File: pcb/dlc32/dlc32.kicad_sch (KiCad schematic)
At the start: 30 parts, among them IC1 74HCT08, IC2 74HCT04, J1 DOOR1, J12 Conn_01x03, J13 Conn_01x03, J2 DOOR2, J3 CHILLER_OK, J7 LASER_AUX, J8 LASER

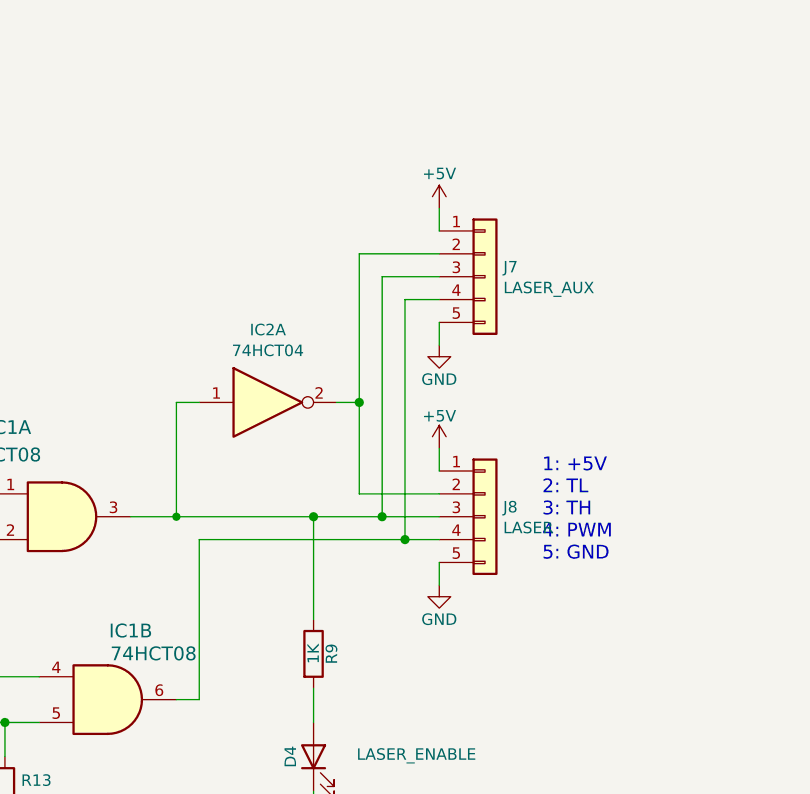
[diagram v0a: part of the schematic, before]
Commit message: Fix footprint for R1.
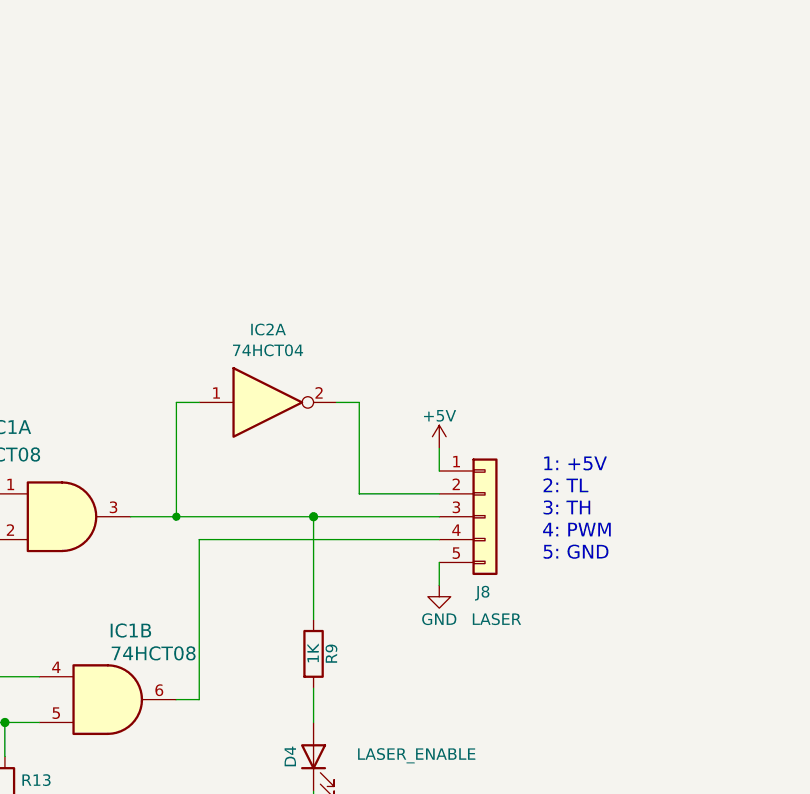
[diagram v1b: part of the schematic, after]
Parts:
- removed J7: LASER_AUX, Connector_JST:JST_XH_B5B-XH-A_1x05_P2.50mm_Vertical, symbol Connector_Generic:Conn_01x05
- J12: value Conn_01x03 -> DOORJMP1
- J13: value Conn_01x03 -> DOORJMP2
- R1: footprint PCM_Resistor_SMD_AKL:R_Array_Concave_4x0603 -> PCM_Resistor_SMD_AKL:R_Array_Convex_4x0603

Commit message: Route some more.
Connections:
- net LASER_EN: now also IC1.12; no longer IC1.1
- net at IC2.1, J8.3 (Pin_3), R9.1: now also IC1.11; no longer IC1.3
- net at C1.1, R8.1: now also IC1.1; no longer IC1.12
- net at IC1.8, IC2.13: now also IC1.2; no longer IC1.13
- new net: IC1.13, IC1.3, IC1.4
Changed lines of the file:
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@@
 		(lib_id "74xx:74LS08")
 		(at 189.23 85.09 0)
-		(unit 1)
+		(unit 4)
 		(exclude_from_sim no)
 		(in_bom yes)
@@
 				(path "/fc0b2ef6-7d8e-4322-8468-8fac0c3c3d07"
 					(reference "IC1")
-					(unit 1)
+					(unit 4)
 				)
 			)
@@
 		(lib_id "74xx:74LS08")
 		(at 157.48 87.63 0)
-		(unit 4)
+		(unit 1)
 		(exclude_from_sim no)
 		(in_bom yes)
@@
 				(path "/fc0b2ef6-7d8e-4322-8468-8fac0c3c3d07"
 					(reference "IC1")
-					(unit 4)
-				)
-			)
+					(unit 1)
+				)
+			)

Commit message: Route.
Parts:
- added H5, H6: MountingHole, MountingHole:MountingHole_3.2mm_M3, symbol Mechanical:MountingHole
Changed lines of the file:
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@@
+	)
+	(symbol
+		(lib_id "Mechanical:MountingHole")
+		(at 58.42 36.83 0)
+		(unit 1)
+		(exclude_from_sim yes)
+		(in_bom no)
+		(on_board yes)
+		(dnp no)
+		(fields_autoplaced yes)
+		(property "Reference" "H6"
+			(at 60.96 35.5599 0)
+			(effects
+				(font
+					(size 1.27 1.27)
+				)
+				(justify left)
+			)
+		)
+		(property "Value" "MountingHole"
+			(at 60.96 38.0999 0)
+			(effects
+				(font
+					(size 1.27 1.27)
+				)
+				(justify left)
+			)
+		)
+		(property "Footprint" "MountingHole:MountingHole_3.2mm_M3"
+			(at 58.42 36.83 0)
+			(effects
+				(font
+					(size 1.27 1.27)
+				)
+				(hide yes)
+			)
+		)
+		(property "Datasheet" "~"
+			(at 58.42 36.83 0)
+			(effects
+				(font
+					(size 1.27 1.27)
+				)
+				(hide yes)
+			)
+		)
+		(property "Description" "Mounting Hole without connection"
+			(at 58.42 36.83 0)
+			(effects
+				(font
+					(size 1.27 1.27)
+				)
+				(hide yes)
+			)
+		)
+		(instances
+			(project "dlc32"
+				(path "/fc0b2ef6-7d8e-4322-8468-8fac0c3c3d07"
+					(reference "H6")
+					(unit 1)
+				)
+			)
+		)
 	)
 	(symbol
@@
 					(unit 1)
 				)
+			)
+		)
+	)
+	(symbol
+		(lib_id "Mechanical:MountingHole")
+		(at 58.42 30.48 0)
+		(unit 1)
+		(exclude_from_sim yes)
+		(in_bom no)
+		(on_board yes)
+		(dnp no)
+		(fields_autoplaced yes)
+		(property "Reference" "H5"
+			(at 60.96 29.2099 0)
+			(effects
+				(font
+					(size 1.27 1.27)
+				)
+				(justify left)
+			)
+		)
+		(property "Value" "MountingHole"
+			(at 60.96 31.7499 0)
+			(effects
+				(font
+					(size 1.27 1.27)
+				)
+				(justify left)
+			)
+		)
+		(property "Footprint" "MountingHole:MountingHole_3.2mm_M3"
+			(at 58.42 30.48 0)
+			(effects
+				(font
+					(size 1.27 1.27)
+				)
+				(hide yes)
+			)
+		)
+		(property "Datasheet" "~"
+			(at 58.42 30.48 0)
+			(effects
+				(font
+					(size 1.27 1.27)
+				)
+				(hide yes)
+			)
+		)
+		(property "Description" "Mounting Hole without connection"
+			(at 58.42 30.48 0)
+			(effects
+				(font
+					(size 1.27 1.27)
+				)
+				(hide yes)
+			)
+		)
+		(instances
+			(project "dlc32"
+				(path "/fc0b2ef6-7d8e-4322-8468-8fac0c3c3d07"
+					(reference "H5")
+					(unit 1)
+				)

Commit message: Make pretty.
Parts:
- D3: value LED -> CHILLER OK
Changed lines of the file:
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@@
 			)
 		)
-		(property "Value" "LED"
+		(property "Value" "CHILLER OK"
 			(at 112.0775 62.23 0)
 			(effects

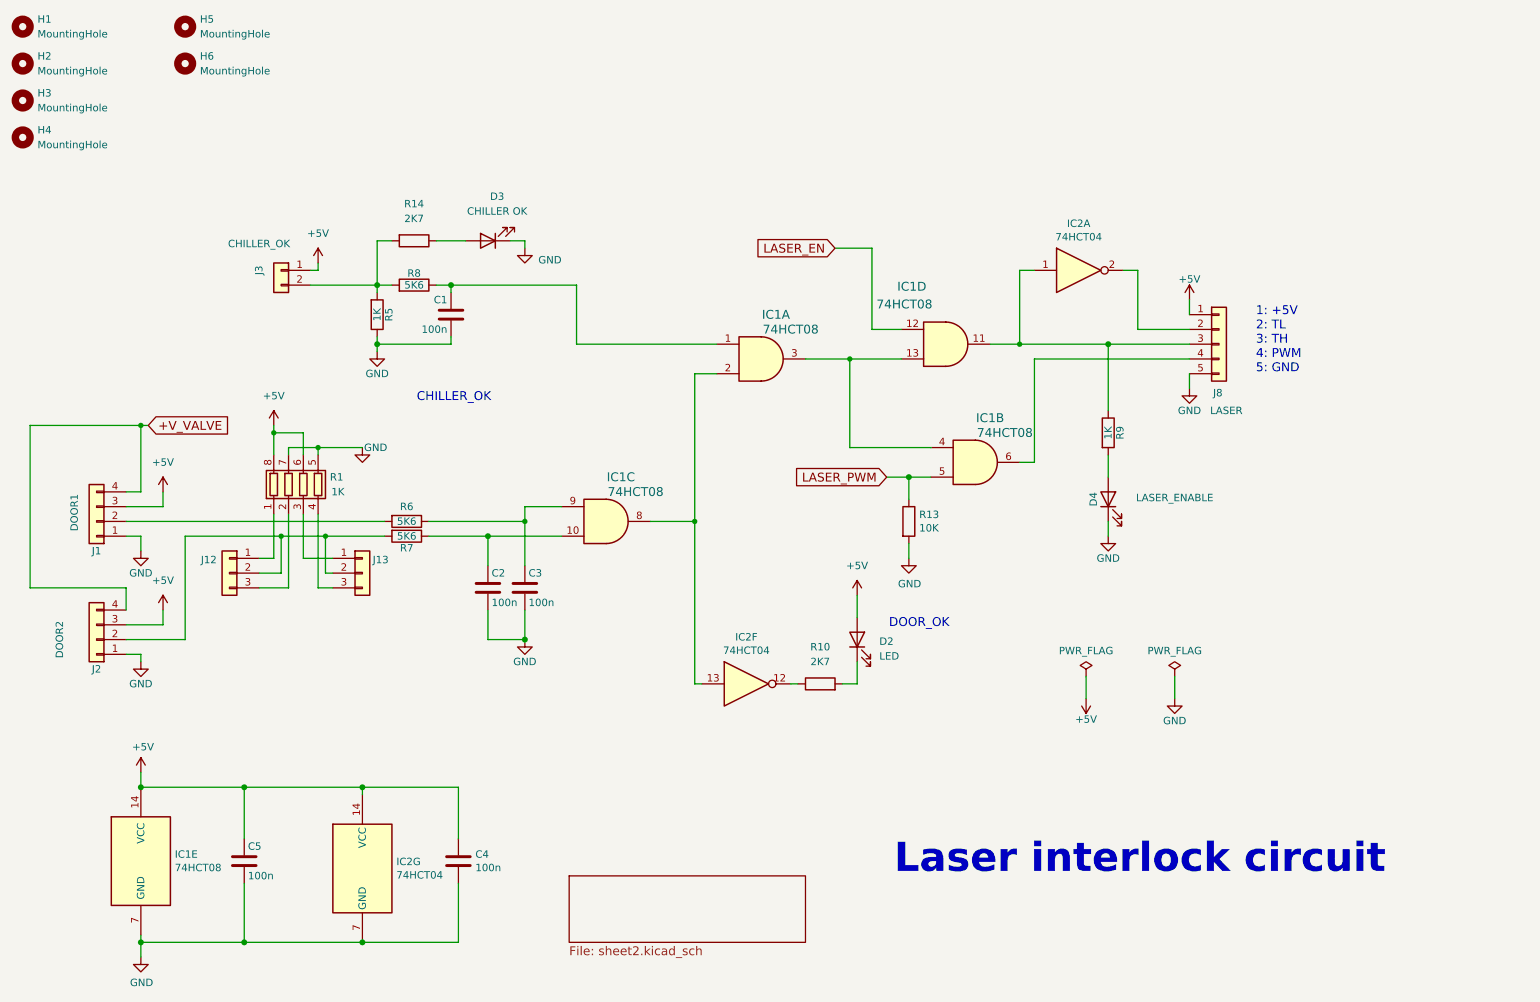
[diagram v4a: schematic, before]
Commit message: Use Schmitt triggers. Add clamping diodes, test point.
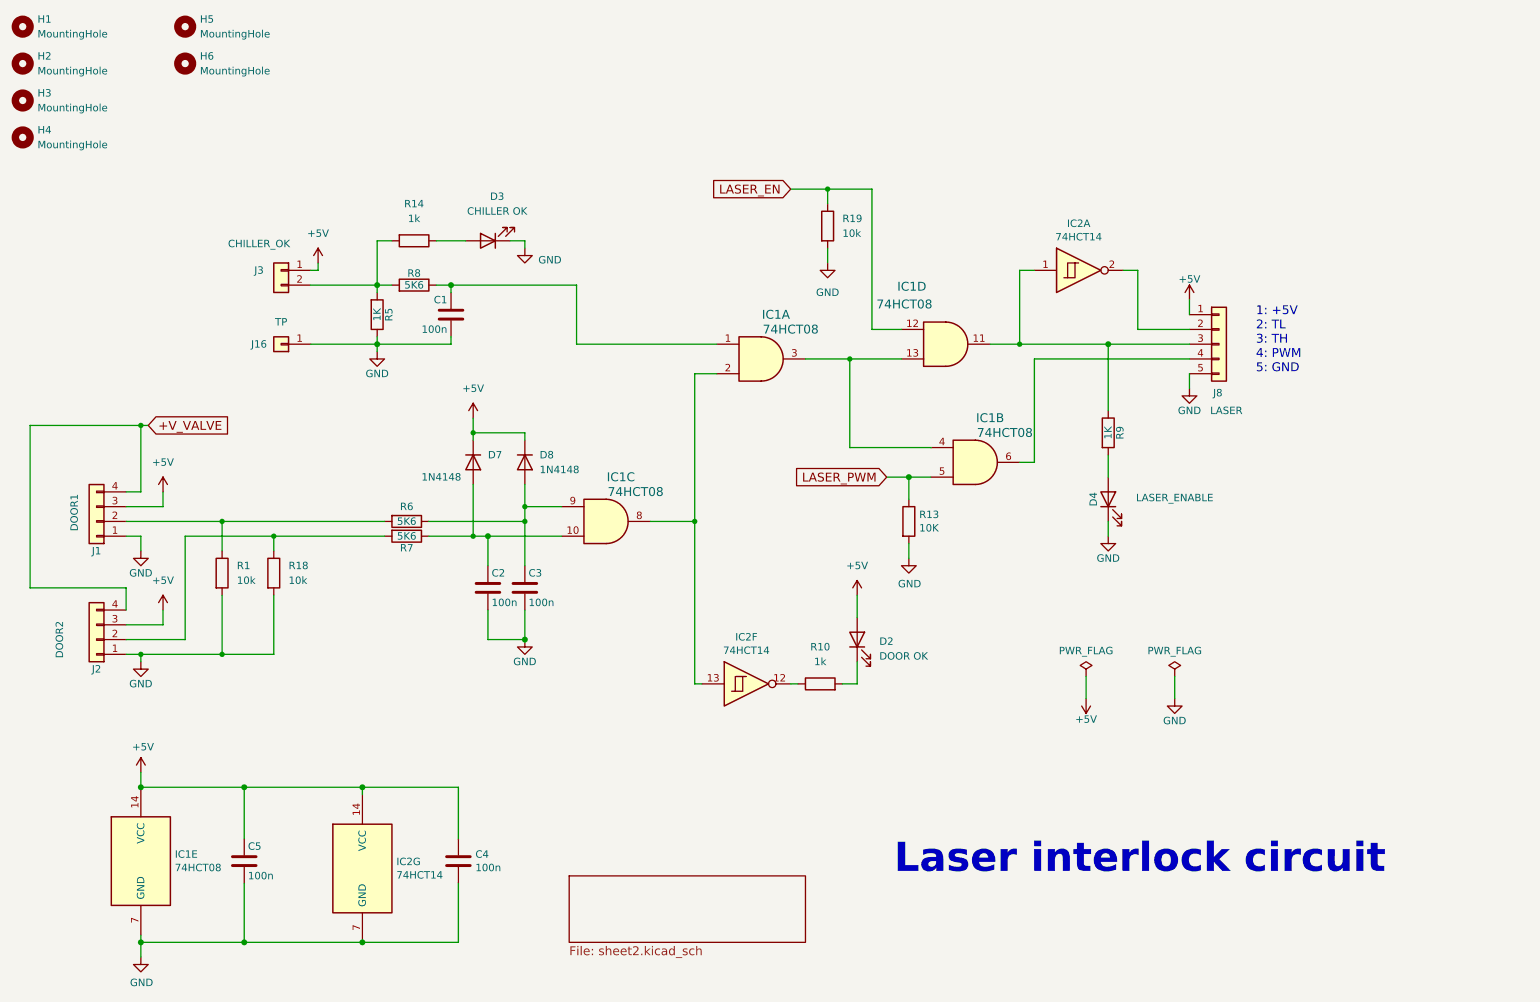
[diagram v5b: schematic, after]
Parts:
- removed J12: DOORJMP1, Connector_PinHeader_2.54mm:PinHeader_1x03_P2.54mm_Vertical, symbol Connector_Generic:Conn_01x03
- removed J13: DOORJMP2, Connector_PinHeader_2.54mm:PinHeader_1x03_P2.54mm_Vertical, symbol Connector_Generic:Conn_01x03
- removed R1: 1K, PCM_Resistor_SMD_AKL:R_Array_Convex_4x0603, symbol Device:R_Pack04
- added D7, D8: 1N4148, PCM_Diode_SMD_AKL:D_MiniMELF, symbol Device:D
- added J16: TP, TestPoint:TestPoint_Loop_D1.80mm_Drill1.0mm_Beaded, symbol Connector_Generic:Conn_01x01
- added R1, R18, R19: 10k, PCM_Resistor_SMD_AKL:R_0603_1608Metric, symbol Device:R
- D2: value LED -> DOOR OK
- IC2: value 74HCT04 -> 74HCT14; symbol 74xx:74HCT04 -> 74xx:74HC14
- R10, R14: value 2K7 -> 1k
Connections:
- net +5V: now also D7.1 (K), D8.1 (K)
- net GND: now also J16.1 (Pin_1), R1.2, R18.2, R19.2
- net LASER_EN: now also R19.1
- net at C3.1, IC1.9, R6.1: now also D8.2 (A)
- net at J1.2 (Pin_2), R6.2: now also R1.1
- net at C2.1, IC1.10, R7.1: now also D7.2 (A)
- net at J2.2 (Pin_2), R7.2: now also R18.1
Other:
- note removed: "CHILLER_OK"
- note removed: "DOOR_OK"

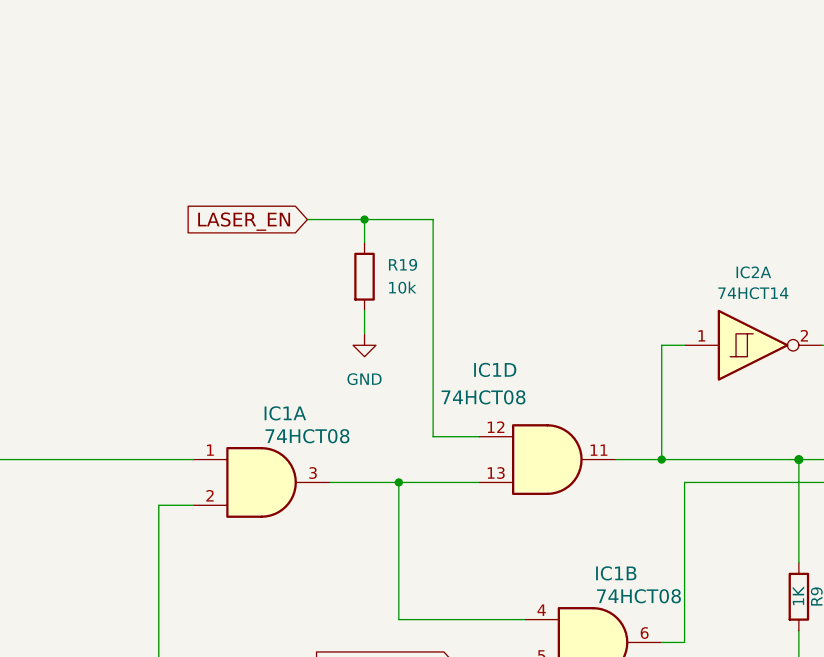
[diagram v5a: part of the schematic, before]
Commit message: Eliminate LASER_EN.
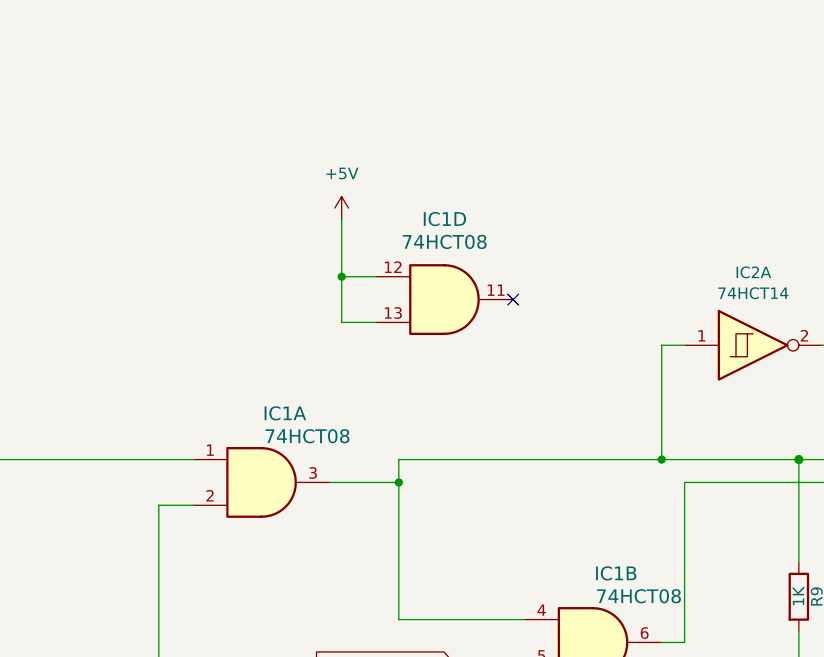
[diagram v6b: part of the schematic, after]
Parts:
- removed R19: 10k, PCM_Resistor_SMD_AKL:R_0603_1608Metric, symbol Device:R
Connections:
- net LASER_EN is gone; now on net +5V: IC1.12
- net +5V: now also IC1.13
- net at IC2.1, J8.3 (Pin_3), R9.1: now also IC1.3, IC1.4; no longer IC1.11
- no-connect marks 0 -> 1
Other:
- moved on the sheet: IC1D

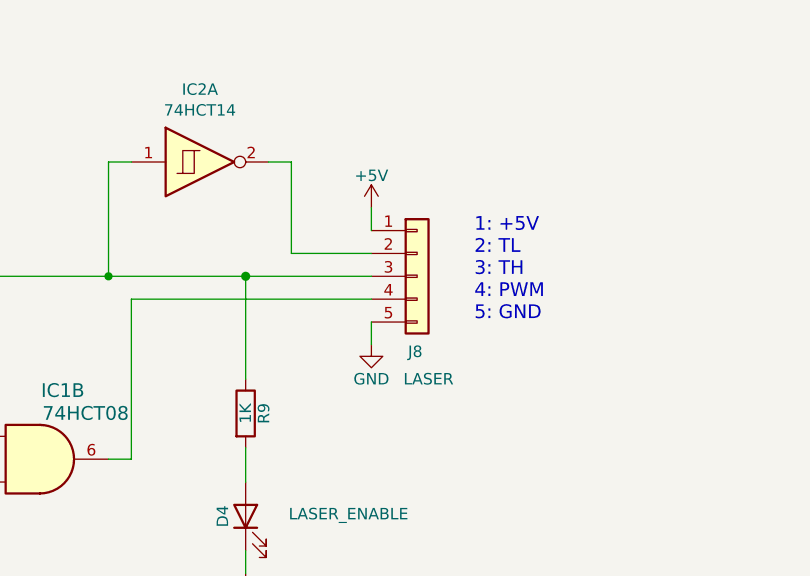
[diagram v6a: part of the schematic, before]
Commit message: Update laser connector, prevent fan activation on startup.
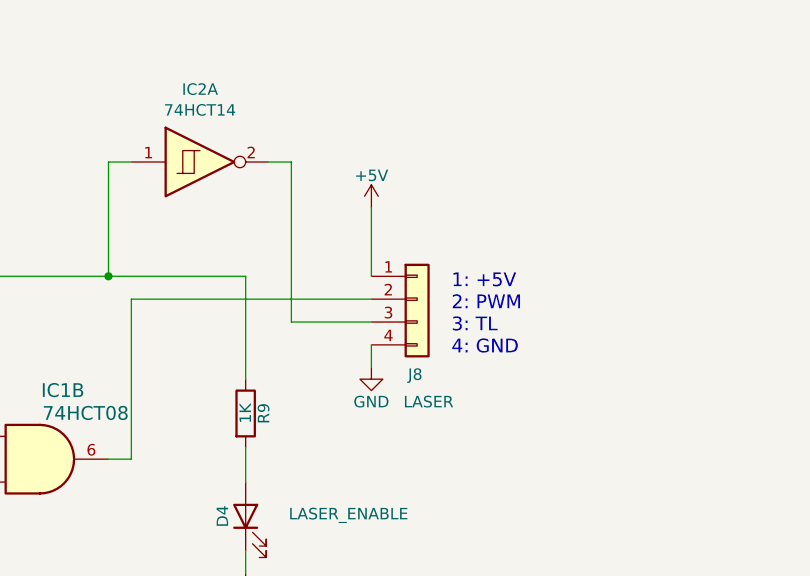
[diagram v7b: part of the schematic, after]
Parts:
- J8: symbol Connector_Generic:Conn_01x05 -> Connector_Generic:Conn_01x04
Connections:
- net GND: now also J8.4 (Pin_4); no longer J8.5 (Pin_5)
- net at IC1.3, IC1.4, IC2.1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: no longer J8.3 (Pin_3)
- net at IC1.6: now also J8.2 (Pin_2); no longer J8.4 (Pin_4)
- net at IC2.2: now also J8.3 (Pin_3); no longer J8.2 (Pin_2)
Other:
- note added: "1: +5V 2: PWM 3: TL 4: GND"
- note removed: "1: +5V 2: TL 3: TH 4: PWM 5: GND"
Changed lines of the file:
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@@
 		)
 	)
-	(text "1: +5V\n2: TL\n3: TH\n4: PWM\n5: GND"
+	(text "1: +5V\n2: PWM\n3: TL\n4: GND"
 		(exclude_from_sim no)
-		(at 242.57 90.17 0)
+		(at 240.03 93.98 0)
 		(effects
 			(font
@@
 	)
 	(junction
-		(at 217.17 85.09)
-		(diameter 1.016)
-		(color 0 0 0 0)
-	)
-	(junction
 		(at 107.95 118.11)
 		(diameter 0)
@@
 	(wire
 		(pts
+			(xy 222.25 90.17) (xy 231.14 90.17)
+		)
+		(stroke
+			(width 0)
+			(type solid)
+		)
+	)
+	(wire
+		(pts
 			(xy 165.1 87.63) (xy 172.72 87.63)
 		)
@@
 	(wire
 		(pts
-			(xy 231.14 77.47) (xy 231.14 80.01)
-		)
-		(stroke
-			(width 0)
-			(type solid)
-		)
-	)
-	(wire
-		(pts
 			(xy 105.41 177.8) (xy 105.41 187.96)
 		)
@@
 	(wire
 		(pts
+			(xy 231.14 77.47) (xy 231.14 85.09)
+		)
+		(stroke
+			(width 0)
+			(type solid)
+		)
+	)
+	(wire
+		(pts
 			(xy 166.37 69.85) (xy 170.18 69.85)
 		)
@@
 	(wire
 		(pts
-			(xy 149.86 85.09) (xy 125.73 85.09)
+			(xy 231.14 92.71) (xy 231.14 95.25)
 		)
 		(stroke
@@
 	(wire
 		(pts
-			(xy 116.84 100.33) (xy 107.95 100.33)
+			(xy 149.86 85.09) (xy 125.73 85.09)
 		)
 		(stroke
@@
 	(wire
 		(pts
-			(xy 116.84 113.03) (xy 116.84 115.57)
+			(xy 116.84 100.33) (xy 107.95 100.33)
 		)
 		(stroke
@@
 	(wire
 		(pts
-			(xy 217.17 115.57) (xy 217.17 118.11)
+			(xy 116.84 113.03) (xy 116.84 115.57)
 		)
 		(stroke
 			(width 0)
-			(type solid)
+			(type default)
 		)
 	)
 	(wire
 		(pts
-			(xy 217.17 85.09) (xy 231.14 85.09)
+			(xy 217.17 115.57) (xy 217.17 118.11)
 		)
 		(stroke
@@
 	(wire
 		(pts
-			(xy 222.25 82.55) (xy 231.14 82.55)
-		)
-		(stroke
-			(width 0)
-			(type solid)
-		)
-	)
-	(wire
-		(pts
 			(xy 50.8 110.49) (xy 48.26 110.49)
 		)
@@
 	(wire
 		(pts
-			(xy 222.25 72.39) (xy 222.25 82.55)
-		)
-		(stroke
-			(width 0)
-			(type solid)
-		)
-	)
-	(wire
-		(pts
-			(xy 231.14 90.17) (xy 231.14 92.71)
+			(xy 222.25 72.39) (xy 222.25 90.17)
 		)
 		(stroke
@@
 	(symbol
 		(lib_id "power:GND")
-		(at 231.14 92.71 0)
+		(at 231.14 95.25 0)
 		(unit 1)
 		(exclude_from_sim no)
@@
 		(dnp no)
 		(property "Reference" "#PWR05"
-			(at 231.14 99.06 0)
+			(at 231.14 101.6 0)
 			(effects
 				(font
@@
 		)
 		(property "Value" "GND"
-			(at 231.14 96.52 0)
+			(at 231.14 99.06 0)
 			(effects
 				(font
@@
 		)
 		(property "Footprint" ""
-			(at 231.14 92.71 0)
+			(at 231.14 95.25 0)
 			(effects
 				(font
@@
 		)
 		(property "Datasheet" ""
-			(at 231.14 92.71 0)
+			(at 231.14 95.25 0)
 			(effects
 				(font
@@
 		)
 		(property "Description" "Power symbol creates a global label with name \"GND\" , ground"
-			(at 231.14 92.71 0)
+			(at 231.14 95.25 0)
 			(effects
 				(font
@@
 	)
 	(symbol
-		(lib_id "Connector_Generic:Conn_01x05")
-		(at 236.22 85.09 0)
+		(lib_id "Connector_Generic:Conn_01x04")
+		(at 236.22 87.63 0)
 		(unit 1)
 		(exclude_from_sim no)
@@
 		(dnp no)
 		(property "Reference" "J8"
-			(at 235.204 93.472 0)
+			(at 235.204 96.012 0)
 			(effects
 				(font
@@
 		)
 		(property "Value" "LASER"
-			(at 234.696 96.52 0)
+			(at 234.696 99.06 0)
 			(effects
 				(font
@@
 		)
 		(property "Footprint" "Connector_JST:JST_XH_B5B-XH-A_1x05_P2.50mm_Vertical"
-			(at 236.22 85.09 0)
+			(at 236.22 87.63 0)
 			(effects
 				(font
@@
 		)
 		(property "Datasheet" "~"
-			(at 236.22 85.09 0)
+			(at 236.22 87.63 0)
 			(effects
 				(font
@@
 			)
 		)
-		(property "Description" ""
-			(at 236.22 85.09 0)
+		(property "Description" "Generic connector, single row, 01x04, script generated (kicad-library-utils/schlib/autogen/connector/)"
+			(at 236.22 87.63 0)
 			(effects
 				(font
 					(size 1.27 1.27)
 				)
+				(hide yes)
 			)
 		)
@@
 		(pin "4"
 		)
-		(pin "5"
-		)
 		(instances
